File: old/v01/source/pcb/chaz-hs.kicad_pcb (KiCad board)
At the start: 2 copper layers, 190.5 x 74 mm, 78 parts, among them SW1 SW_Push_45deg, SW10 SW_Push_45deg, SW11 SW_Push_45deg, SW12 SW_Push_45deg, SW13 SW_Push_45deg, SW14 SW_Push_45deg, SW15 SW_Push_45deg, SW16 SW_Push_45deg, SW17 SW_Push_45deg, SW18 SW_Push_45deg, SW19 SW_Push_45deg, SW2 SW_Push_45deg, SW20 SW_Push_45deg, SW21 SW_Push_45deg, SW22 SW_Push_45deg, SW23 SW_Push_45deg, SW24 SW_Push_45deg, SW25 SW_Push_45deg, SW26 SW_Push_45deg, SW27 SW_Push_45deg, SW28 SW_Push_45deg, SW29 SW_Push_45deg, SW3 SW_Push_45deg, SW30 SW_Push_45deg, SW31 SW_Push_45deg, SW32 SW_Push_45deg, SW33 SW_Push_45deg, SW34 SW_Push_45deg, SW35 SW_Push_45deg, SW36 SW_Push_45deg, SW37 SW_Push_45deg, SW4 SW_Push_45deg, SW5 SW_Push_45deg, SW6 SW_Push_45deg, SW7 SW_Push_45deg, SW8 SW_Push_45deg, SW9 SW_Push_45deg, U1 ProMicro

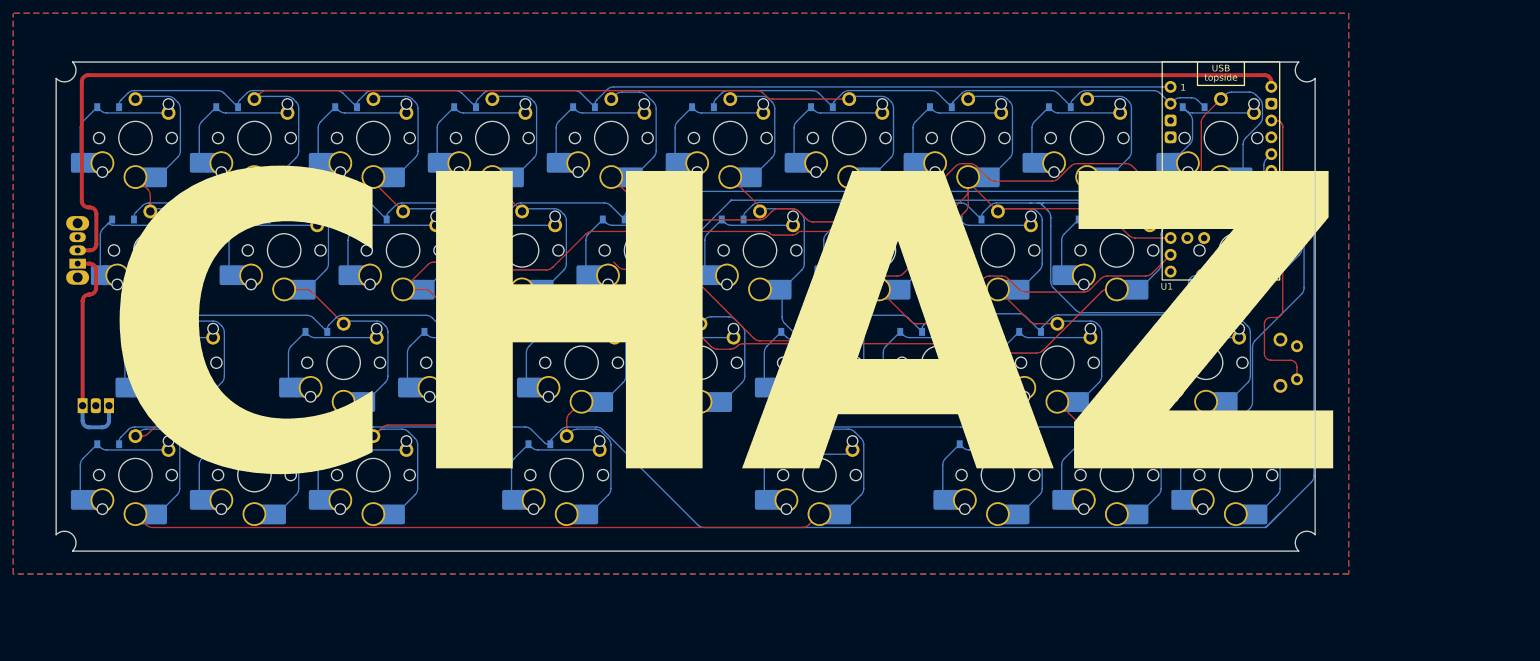
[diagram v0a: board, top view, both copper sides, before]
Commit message: cleaning up routing
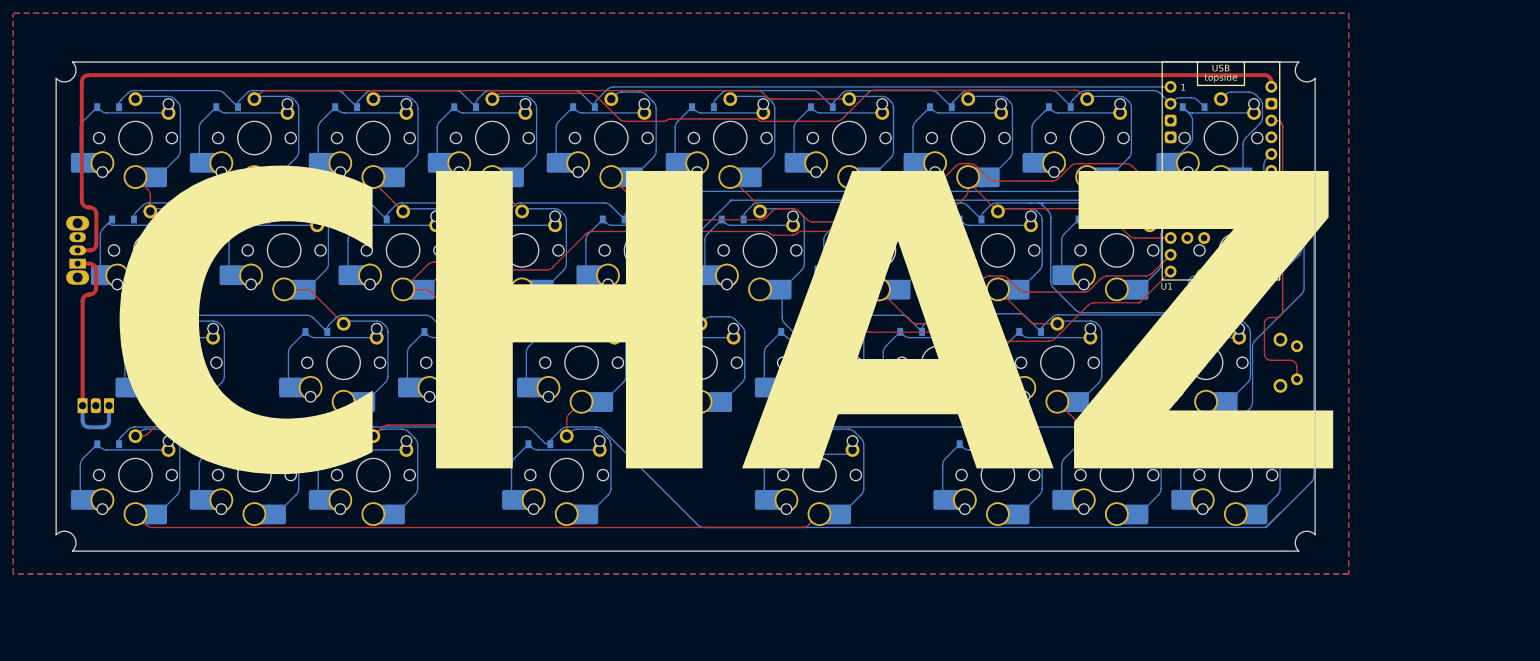
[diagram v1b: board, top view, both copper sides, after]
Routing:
- net /col2: track 416.0 -> 343.6 mm
- net /col0: track 318.0 -> 383.4 mm
- net /col4: track 292.6 -> 273.6 mm
- net /col3: track 238.6 -> 247.8 mm
